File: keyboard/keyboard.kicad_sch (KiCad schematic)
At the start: 32 parts, among them IC100 TC4021BP, J1 Jumper_2_Bridged, J2 Jumper_2_Bridged, J3 Jumper_2_Bridged, J4 Jumper_2_Bridged, J5 Jumper_2_Bridged, J6 Jumper_2_Bridged, J7 Jumper_2_Bridged, SW100 SW_Push, SW101 SW_Push, SW102 SW_Push, SW103 SW_Push, SW104 SW_Push, SW105 SW_Push, SW106 SW_Push, SW107 SW_Push, SW110 SW_Push, SW111 SW_Push, SW112 SW_Push, SW113 SW_Push, SW114 SW_Push, SW115 SW_Push, SW116 SW_Push, SW117 SW_Push, SW120 SIMODESW

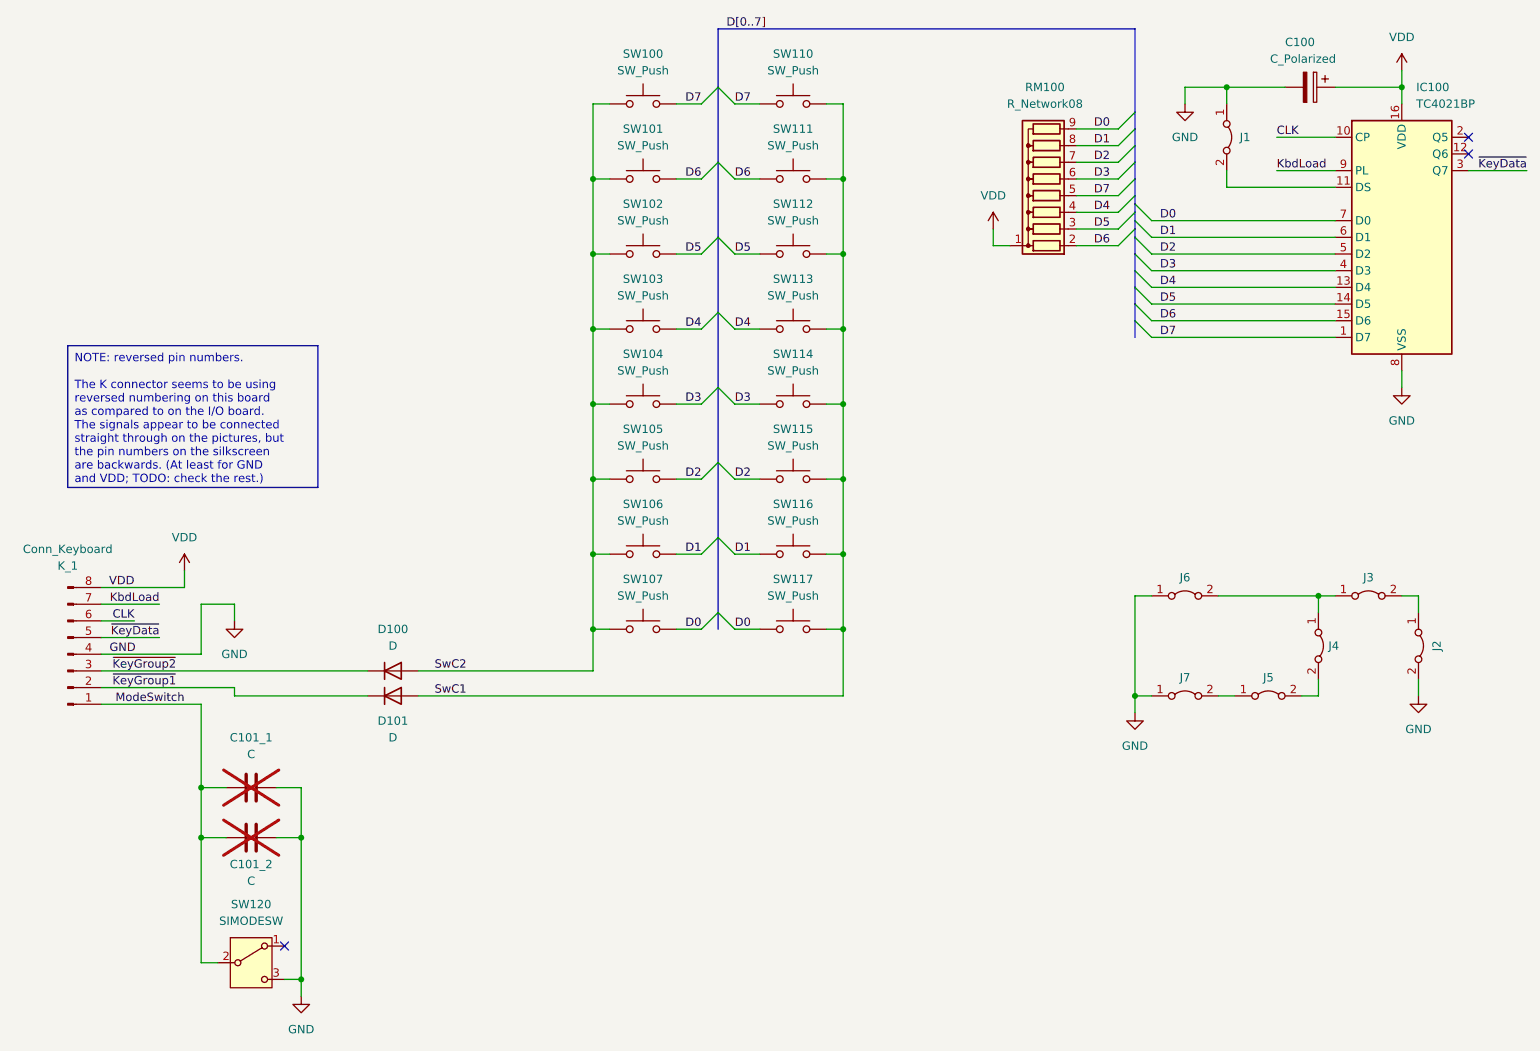
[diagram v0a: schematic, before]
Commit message: Add some notes on the keyboard schematic
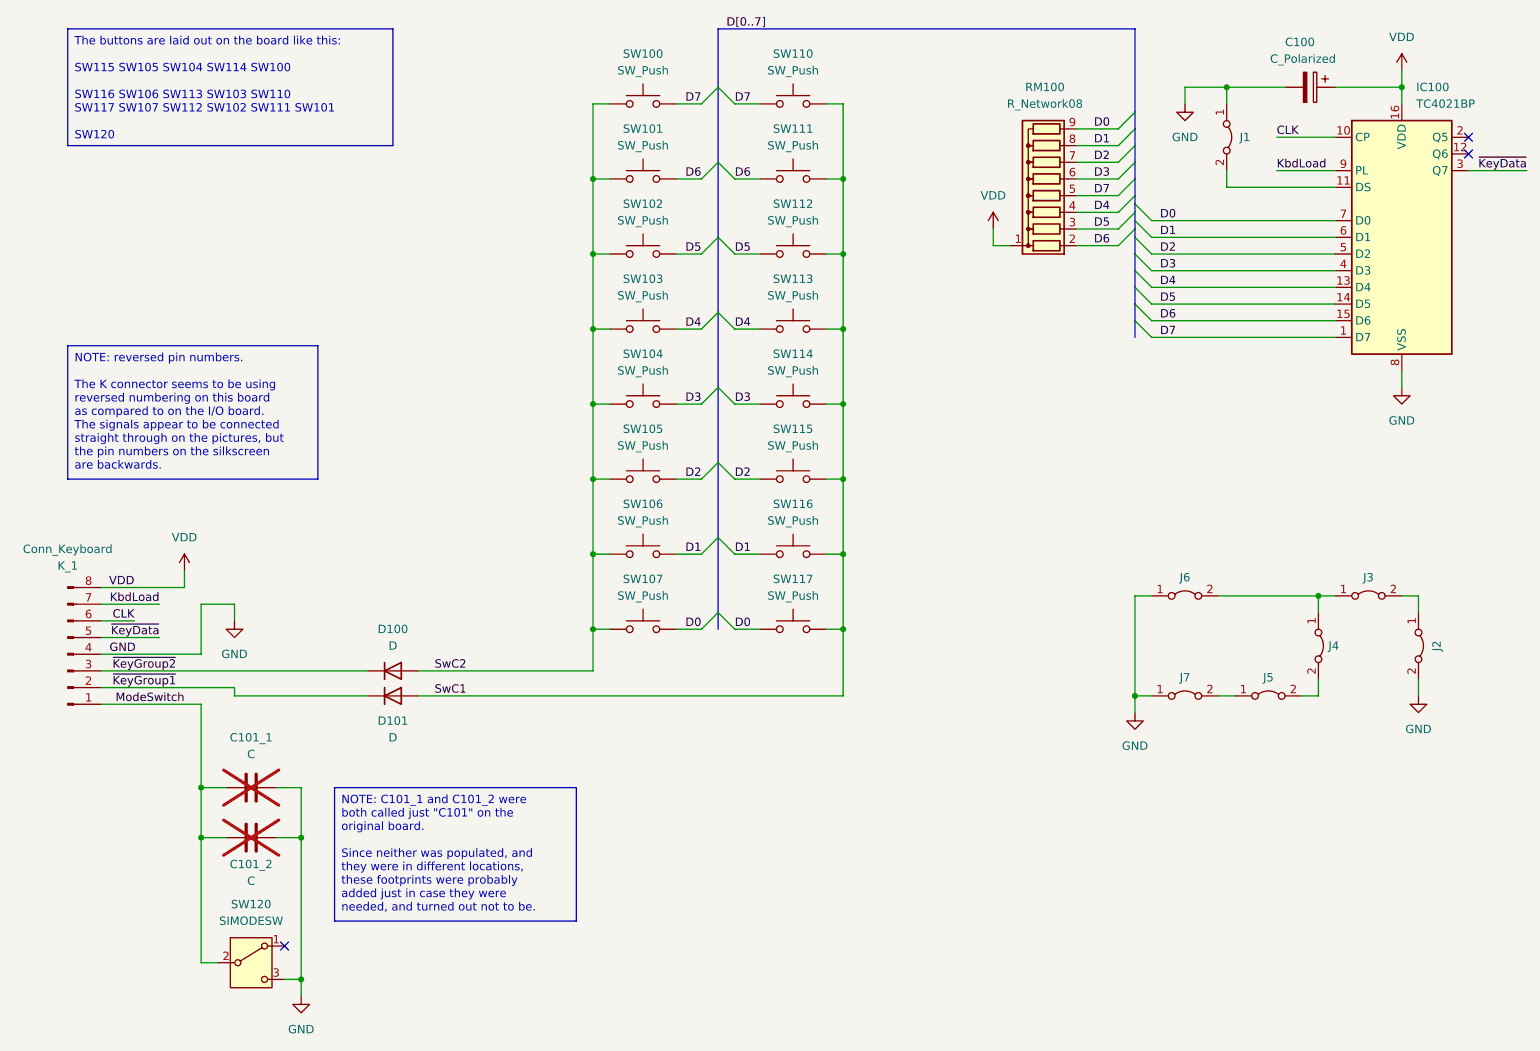
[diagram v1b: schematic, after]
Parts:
- C101_1, C101_2: Note Called "C101" on the original board, but in two locations, 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 -> (none)
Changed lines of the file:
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@@
 		)
 	)
-	(text_box "NOTE: reversed pin numbers.\n\nThe K connector seems to be using reversed numbering on this board as compared to on the I/O board.\nThe signals appear to be connected straight through on the pictures, but the pin numbers on the silkscreen are backwards. (At least for GND and VDD; TODO: check the rest.)"
+	(text_box "The buttons are laid out on the board like this:\n\nSW115 SW105 SW104 SW114 SW100\n\nSW116 SW106 SW113 SW103 SW110\nSW117 SW107 SW112 SW102 SW111 SW101\n\nSW120"
+		(exclude_from_sim no)
+		(at 35.56 30.48 0)
+		(size 49.53 17.78)
+		(stroke
+			(width 0)
+			(type default)
+		)
+		(fill
+			(type none)
+		)
+		(effects
+			(font
+				(size 1.27 1.27)
+			)
+			(justify left top)
+		)
+	)
+	(text_box "NOTE: reversed pin numbers.\n\nThe K connector seems to be using reversed numbering on this board as compared to on the I/O board.\nThe signals appear to be connected straight through on the pictures, but the pin numbers on the silkscreen are backwards."
 		(exclude_from_sim no)
 		(at 35.56 78.74 0)
-		(size 38.1 21.59)
+		(size 38.1 20.32)
+		(stroke
+			(width 0)
+			(type default)
+		)
+		(fill
+			(type none)
+		)
+		(effects
+			(font
+				(size 1.27 1.27)
+			)
+			(justify left top)
+		)
+	)
+	(text_box "NOTE: C101_1 and C101_2 were both called just \"C101\" on the original board.\n\nSince neither was populated, and they were in different locations, these footprints were probably added just in case they were needed, and turned out not to be."
+		(exclude_from_sim no)
+		(at 76.2 146.05 0)
+		(size 36.83 20.32)
 		(stroke
 			(width 0)
@@
 			)
 		)
-		(property "Note" "Called \"C101\" on the original board, but in two locations, so the Ref here adds a suffix to disambiguate."
-			(at 63.5 146.05 90)
-			(effects
-				(font
-					(size 1.27 1.27)
-				)
-				(hide yes)
-			)
-		)
 		(pin "2"
 		)
@@
 			(effects
 				(font
-					(size 1.27 1.27)
-				)
-				(hide yes)
-			)
-		)
-		(property "Note" "Called \"C101\" on the original board, but in two locations, so the Ref here adds a suffix to disambiguate."
-			(at 63.5 153.67 90)
-			(effects
-				(font
